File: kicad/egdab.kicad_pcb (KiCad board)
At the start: 4 copper layers, 93.4 x 99.4 mm, 65 parts, among them J1 Audio-Jack-2_Switch, J2 Conn_02x03_Counter_Clockwise, J3 Conn_02x04_Counter_Clockwise, SW1 SW_DIP_x12, SW2 SW_Push, SW3 SW_Push, SW4 SW_Push, SW5 SW_Push, SW6 SW_SPST, U1 ATtiny1606-S, U2 AS1115-BSST, U3 LM35-D, U4 CAP1296

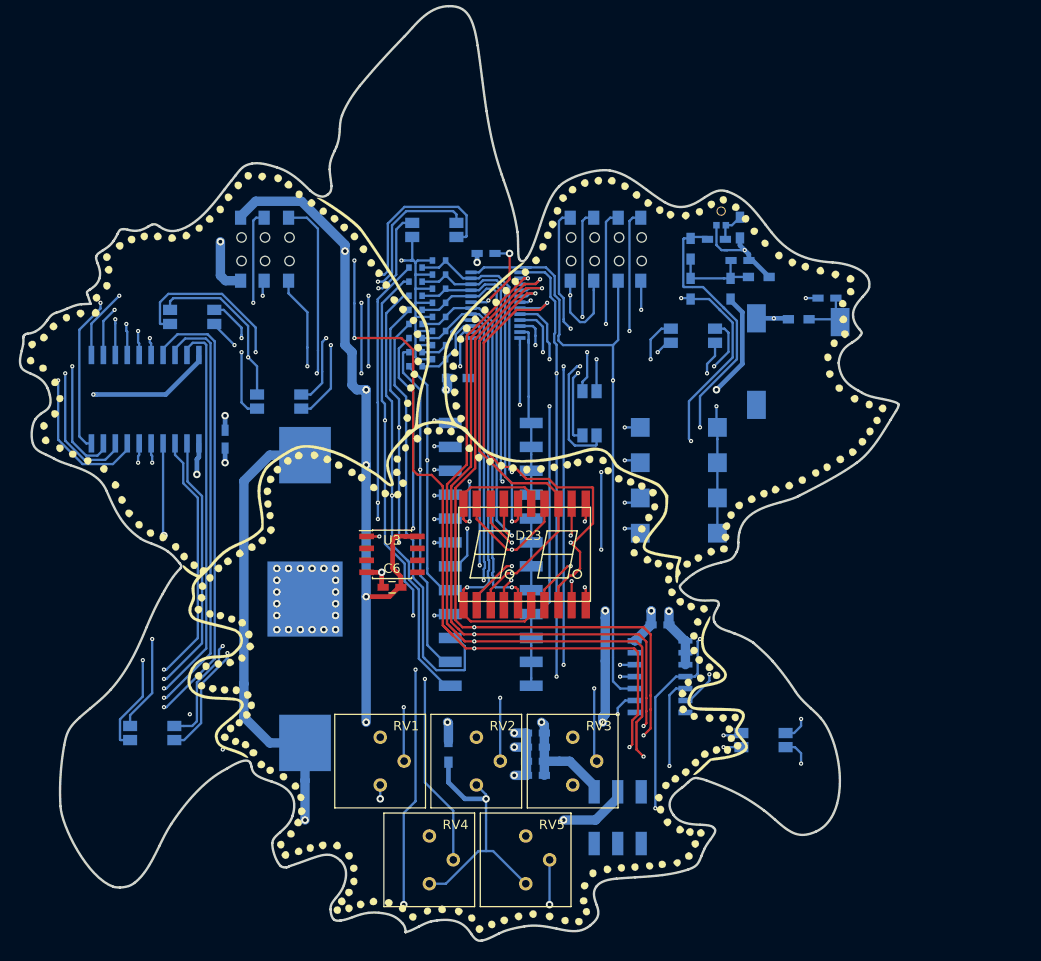
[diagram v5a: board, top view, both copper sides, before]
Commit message: PCB v2 redesign WIP
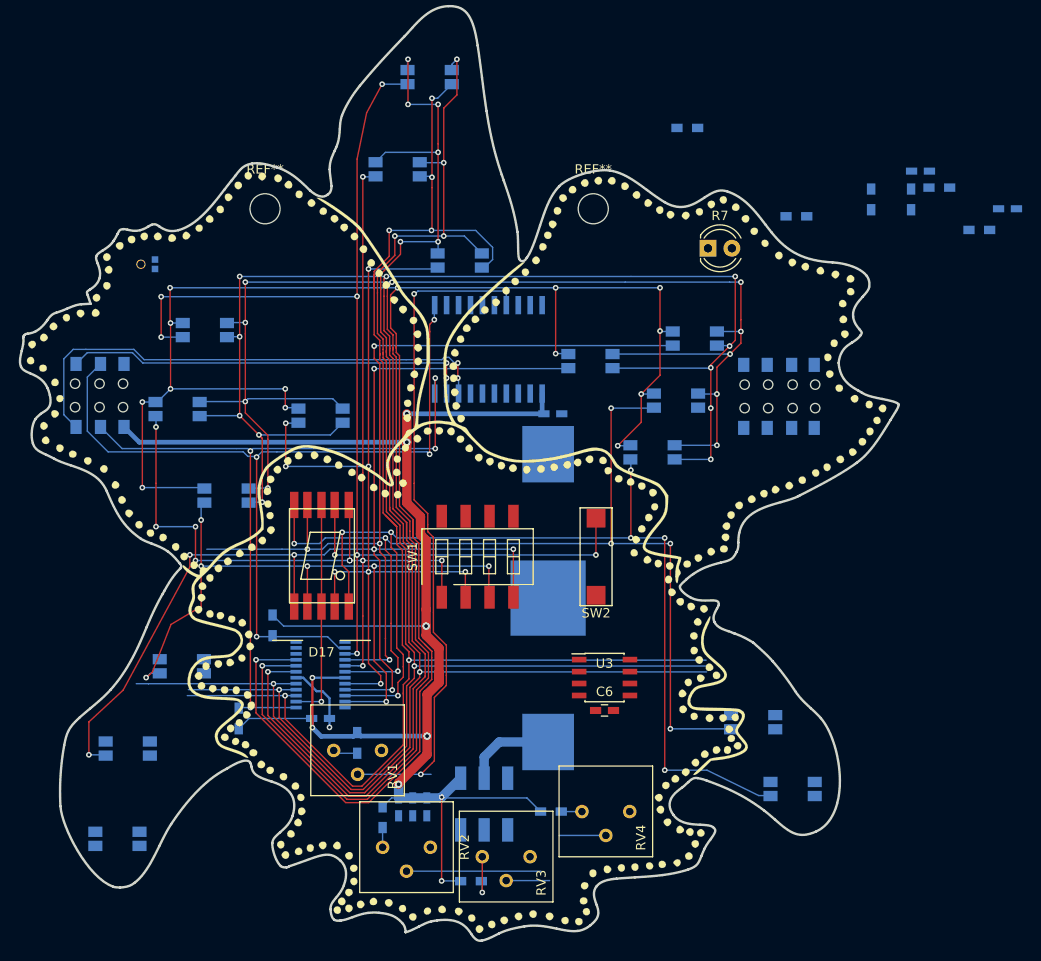
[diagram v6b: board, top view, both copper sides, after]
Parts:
- removed C11: 10uF, Capacitors_SMD:C_0603_HandSoldering
- removed C7, C8: 22uF, Capacitors_SMD:C_0603_HandSoldering
- removed D18, D20, D24: LED_RGB, BBS Components:LED_RGB_SMD_PLCC4_Reverse_XZMDKCBDDG45S
- removed D19, D21, D22: D, Diodes_SMD:D_SOD-523
- removed D23: 7SegmentLED_ACDA02, BBS Components:7SegmentLED_ACDA02
- removed J1: Audio-Jack-2_Switch, BBS Components:sj2-35852b-smt
- removed RV5: R_POT, Potentiometers:Potentiometer_Trimmer_Suntan_TSR-3386P_Horizontal
- removed SW3, SW4, SW5: SW_Push, BBS Components:SW_SPST_SMD_3_6
- removed U4: CAP1296, Housings_SOIC:SOIC-14_3.9x8.7mm_Pitch1.27mm
- added R11: 10K, Resistors_SMD:R_0603_HandSoldering, B.Cu at (173.0, 133.7)
- added R12: 10K, Resistors_SMD:R_0603_HandSoldering, B.Cu at (182.4, 140.5)
- added R13: 10K, Resistors_SMD:R_0603_HandSoldering, B.Cu at (190.9, 133.1)
- added R8: 4K7, Resistors_SMD:R_0603_HandSoldering, B.Cu at (161.3, 113.3)
- added R9: 4K7, Resistors_SMD:R_0603_HandSoldering, B.Cu at (157.7, 123.2)
- added REF**: MountingHole_3.2mm_M3, Mounting_Holes:MountingHole_3.2mm_M3, F.Cu at (195.4, 69.0)
- added REF**: MountingHole_3.2mm_M3, Mounting_Holes:MountingHole_3.2mm_M3, F.Cu at (160.5, 69.0)
- D1, D12, D13, D16, D2, D3, D4, D5, D6, D7, D8, D9: value D -> LED_RGB; footprint Diodes_SMD:D_SOD-523 -> BBS Components:LED_RGB_SMD_PLCC4_Reverse_XZMDKCBDDG45S
- D17: value D -> 7SegmentLED_ACSC02; footprint Diodes_SMD:D_SOD-523 -> BBS Components:7SegmentLED_ACSC02; moved to F.Cu
- R7: value 10K -> R_PHOTO; footprint Resistors_SMD:R_0603_HandSoldering -> LEDs:LED_D4.0mm; moved to F.Cu
- SW1: value SW_DIP_x12 -> SW_DIP_x04; footprint Buttons_Switches_SMD:SW_DIP_x12_W8.61mm_Slide_LowProfile -> Buttons_Switches_SMD:SW_DIP_x4_W8.61mm_Slide_LowProfile; moved to F.Cu
- SW2: moved to F.Cu
- moved D14 71.3 mm to (206.2, 82.8)
- moved D6 64.6 mm to (144.8, 136.0)
- moved MK1 61.4 mm to (147.8, 74.9), turned to 0 degrees
- moved D8 60.2 mm to (216.6, 130.7)
- moved D5 59.6 mm to (145.9, 126.4)
- moved D7 54.4 mm to (212.4, 123.6)
- moved C2 52.5 mm to (166.4, 123.2), turned to 0 degrees
- moved D15 52.2 mm to (204.2, 89.4), turned to 0 degrees
- moved D4 46.6 mm to (151.7, 117.7)
- moved U2 43.5 mm to (166.4, 118.5), turned to 0 degrees
- moved U1 36.9 mm to (184.2, 84.0)
- moved R1 36.1 mm to (205.4, 60.4)
- moved C1 35.0 mm to (191.1, 90.8), turned to 0 degrees
- moved D17 33.8 mm to (166.5, 105.9)
- moved D10 33.3 mm to (151.2, 90.3)
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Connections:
- net /POT1 renamed /P_LUMA
- net /POT2 renamed /P_CHROMA-
- net /POT3 renamed /P_CHROMA+
- net /POT4 renamed /P_TIME
- D1 pad 1: Net-(D1-Pad1) -> /DIG1
- D1 pad 2: /SEGDP -> /SEGA
- D10 pad 1: /DIG0 -> /DIG4
- D10 pad 2: /ALL_SEG -> /SEGB
- D10 pad 3: /DIG2 -> /DIG6
- D10 pad 4: /DIG1 -> /DIG5
- D11 pad 1: /DIG5 -> /DIG4
- D11 pad 2: /ALL_SEG -> /SEGC
- D11 pad 3: /DIG7 -> /DIG6
- D11 pad 4: /DIG6 -> /DIG5
- D12 pad 1: /ALL_SEG -> /DIG4
- D12 pad 2: /SEGG -> /SEGD
- D13 pad 1: /ALL_SEG -> /DIG4
- D13 pad 2: /SEGF -> /SEGE
- D14 pad 1: /DIG0 -> /DIG4
- D14 pad 2: /ALL_SEG -> /SEGF
- D14 pad 3: /DIG2 -> /DIG6
- D14 pad 4: /DIG1 -> /DIG5
- D15 pad 1: /DIG5 -> /DIG4
- D15 pad 2: /ALL_SEG -> /SEGG
- D15 pad 3: /DIG7 -> /DIG6
- D15 pad 4: /DIG6 -> /DIG5
- D16 pad 1: /ALL_SEG -> /DIG4
- D16 pad 2: /SEGE -> /SEGDP
- D17 pad 1: /ALL_SEG -> /SEGE
- D2 pad 1: Net-(D2-Pad1) -> /DIG1
- D2 pad 2: /SEGG -> /SEGB
- D3 pad 1: Net-(D3-Pad1) -> /DIG1
- D3 pad 2: /SEGF -> /SEGC
- D4 pad 1: Net-(D4-Pad1) -> /DIG1
- D4 pad 2: /SEGE -> /SEGD
- D5 pad 1: Net-(D5-Pad1) -> /DIG1
- D5 pad 2: /SEGD -> /SEGE
- D6 pad 1: Net-(D6-Pad1) -> /DIG1
- D6 pad 2: /SEGC -> /SEGF
- D7 pad 1: Net-(D7-Pad1) -> /DIG1
- D7 pad 2: /SEGB -> /SEGG
- D8 pad 1: Net-(D8-Pad1) -> /DIG1
- D8 pad 2: /SEGA -> /SEGDP
- D9 pad 1: /ALL_SEG -> /DIG4
- D9 pad 2: /SEGDP -> /SEGA
- MK1 pad 2: Net-(C11-Pad1) -> Net-(C9-Pad1)
- R10 pad 1: /MIC -> /PHOTO
- R10 pad 2: Net-(C10-Pad2) -> GND
- R7 pad 1: Net-(C11-Pad1) -> +3V0
- R7 pad 2: GND -> /PHOTO
- RV2 pad 1: Net-(R2-Pad1) -> Net-(R11-Pad1)
- RV3 pad 1: Net-(R2-Pad1) -> Net-(R12-Pad1)
- RV4 pad 1: Net-(R2-Pad1) -> Net-(R13-Pad1)
- SW1 pad 1: /KEYA -> /SEGB
- SW1 pad 2: /KEYA -> /SEGC
- SW1 pad 3: /KEYA -> /SEGD
- SW1 pad 4: /KEYA -> /SEGE
- SW2 pad 1: /KEYB -> /SEGA
- SW2 pad 2: Net-(D5-Pad1) -> /KEYA
- U1 pad 3: /POT5 -> /PHOTO
- U1 pad 6: /MIC -> Net-(U1-Pad6)
- U2 pad 12: /KEYB -> Net-(U2-Pad12)
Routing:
- net /ALL_SEG: track 235.8 -> 0.00 mm, vias 11 -> 0
- net /DIG0: track 175.8 -> 23.6 mm, vias 6 -> 1
- net /DIG4: track 62.9 -> 214.0 mm, vias 3 -> 12
- net UI_INTERRUPT: track 144.1 -> 0.00 mm, vias 2 -> 0
- net /DIG5: track 86.4 -> 219.0 mm, vias 4 -> 11
- net /DIG6: track 100.1 -> 218.9 mm, vias 5 -> 15
- net /DIG3: track 47.1 -> 164.4 mm, vias 2 -> 8
- net /POT5: track 99.2 -> 0.00 mm, vias 4 -> 0
- net /AUDIO: track 96.3 -> 0.00 mm, vias 4 -> 0
- net /MIC: track 91.5 -> 0.00 mm, vias 2 -> 0
- net /P_CHROMA+: track 95.2 -> 4.62 mm, vias 2 -> 0
- net /SEGE: track 51.7 -> 132.7 mm, vias 3 -> 7
- net /SEGA: track 55.5 -> 129.5 mm, vias 3 -> 8
- net /KEYB: track 73.9 -> 0.00 mm, vias 3 -> 0
- net /BAT+: track 83.5 -> 9.71 mm, vias 2 -> 0
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- removed copper zone on In2.Cu, net GND
- removed copper zone on In2.Cu, net TOUCH1
- removed copper zone on In2.Cu, net TOUCH2
- removed copper zone on In2.Cu, net TOUCH_GUARD
- removed copper zone on In2.Cu, net TOUCH_PROX
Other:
- net class Default: trace_width 0.25 -> 0.15; via_dia 0.45 -> 0.6; via_drill 0.2 -> 0.3
- net class Power: via_dia 0.45 -> 0.6; via_drill 0.2 -> 0.3
- rule trace_min: 0.2 -> 0.15
- rule via_min_size: 0.45 -> 0.6
- board text added: "BBS 2020 v3"
- board text removed: "A"
- board text removed: "B"
- board text removed: "BBS 2019 v2"
- board text removed: "C"
- board text removed: "D"
- board text removed: "E"
- board text removed: "F"
- board text removed: "G"
- board text removed: "H"
- board text removed: "I"
- board text removed: "J"
- board text removed: "K"
- board text removed: "L"

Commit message: V3 ordered
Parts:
- moved C9 87.5 mm to (152.2, 75.3), turned to 0 degrees
- moved R3 86.5 mm to (150.1, 76.9)
- moved R5 77.8 mm to (155.1, 76.9), turned to 180 degrees
- moved C10 71.9 mm to (159.3, 76.9)
- moved R1 71.0 mm to (158.1, 113.3), turned to 270 degrees
- moved R4 69.2 mm to (160.4, 75.3), turned to 180 degrees
- moved R6 69.1 mm to (156.2, 75.3), turned to 0 degrees
- moved R10 7.33 mm to (217.7, 77.1)
- moved C6 6.85 mm to (196.5, 115.5)
- moved C2 6.70 mm to (173.1, 123.0)
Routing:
- net GND: track 7.55 -> 163.7 mm, vias 1 -> 27
- net +3V0: track 172.1 -> 265.9 mm, vias 9 -> 12
- net UI_INTERRUPT: track 0.00 -> 89.3 mm, vias 0 -> 4
- net /P_CHROMA+: track 4.62 -> 65.7 mm, vias 0 -> 2
- net /P_CHROMA-: track 14.3 -> 72.9 mm, vias 0 -> 2
- net SPI_SS: track 0.00 -> 57.2 mm, vias 0 -> 2
- net /KEYA: track 0.00 -> 55.9 mm, vias 0 -> 7
- net /P_TIME: track 4.98 -> 58.3 mm, vias 0 -> 2
- net /DIG1: track 156.1 -> 205.9 mm, vias 6 -> 10
- net /AUDIO: track 0.00 -> 46.9 mm, vias 0 -> 4
- net /SEGF: track 93.8 -> 139.7 mm, vias 4 -> 6
- net SPI_SCK: track 0.00 -> 45.1 mm, vias 0 -> 2
- net SPI_MISO: track 0.00 -> 43.6 mm, vias 0 -> 2
- net /DIG3: track 164.4 -> 207.3 mm, vias 8 -> 13
- net /PHOTO: track 0.00 -> 42.6 mm, vias 0 -> 2
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- added copper zone on F.Cu, net GND
